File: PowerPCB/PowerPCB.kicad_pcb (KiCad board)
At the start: 2 copper layers, 41 parts, among them J1 Conn_01x03_Male, J2 Conn_01x10_Male, J5 Conn_01x07_Male, K1 1721081-5, K2 1721081-5, K3 1721081-5, Q1 Q_PMOS_DGS, U1 NCP1117-3.3_SOT223, U2 STM32F413ZHTx, U3 NCP1117-5.0_SOT223, U4 MCP2562-E-P, U5 MCP2562-E-P

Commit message: Testing branch
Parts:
- moved J5 30.6 mm to (171.4, 50.8)
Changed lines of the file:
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@@
     (solder_mask_min_width 0.25)
     (aux_axis_origin 0 0)
-    (visible_elements 7FFFFFFF)
+    (visible_elements 7FFFF7FF)
     (pcbplotparams
       (layerselection 0x010fc_ffffffff)
@@
   )
   (module Connector_PinHeader_2.54mm:PinHeader_1x07_P2.54mm_Horizontal (layer F.Cu)
-    (at 140.97 48.26)
+    (at 171.45 50.8)
     (descr "Through hole angled pin header, 1x07, 2.54mm pitch, 6mm pin length, single row")
     (tags "Through hole angled pin header THT 1x07 2.54mm single row")

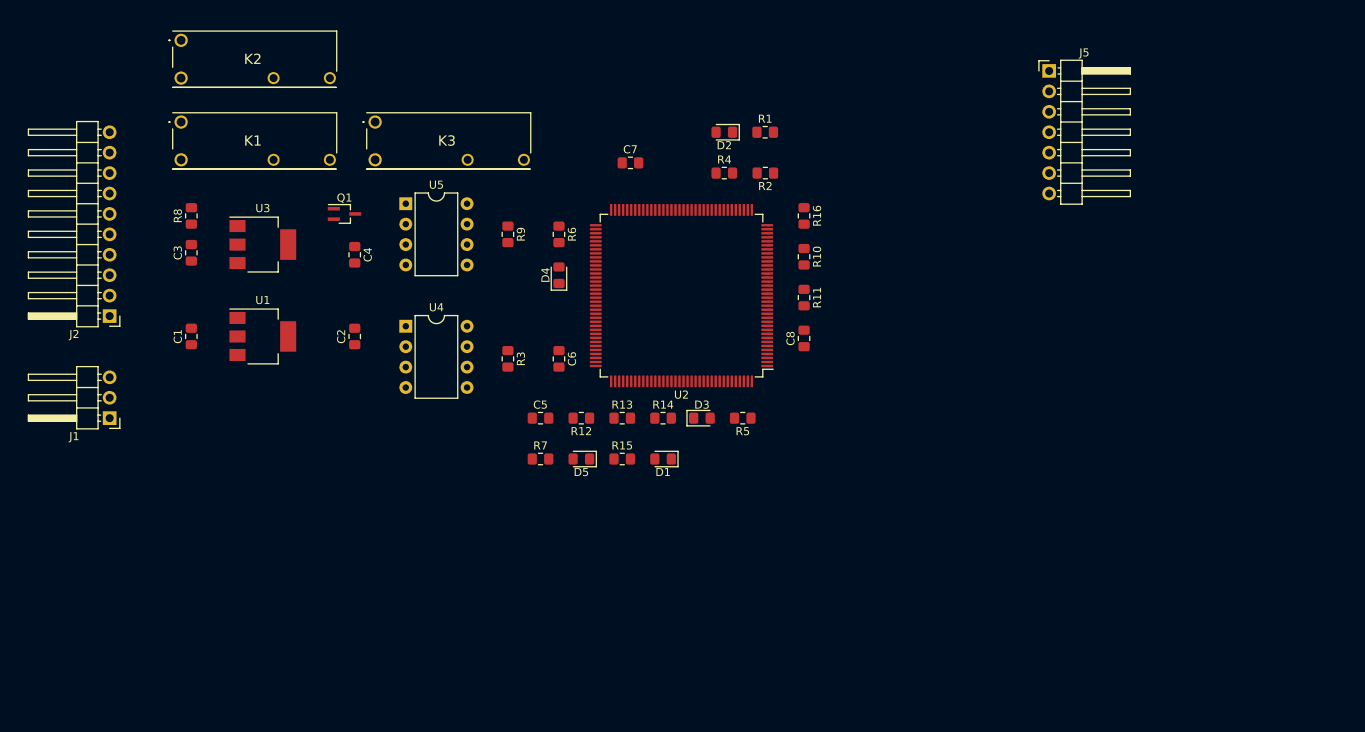
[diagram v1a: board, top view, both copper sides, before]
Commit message: Imported input protection components to PCBnew
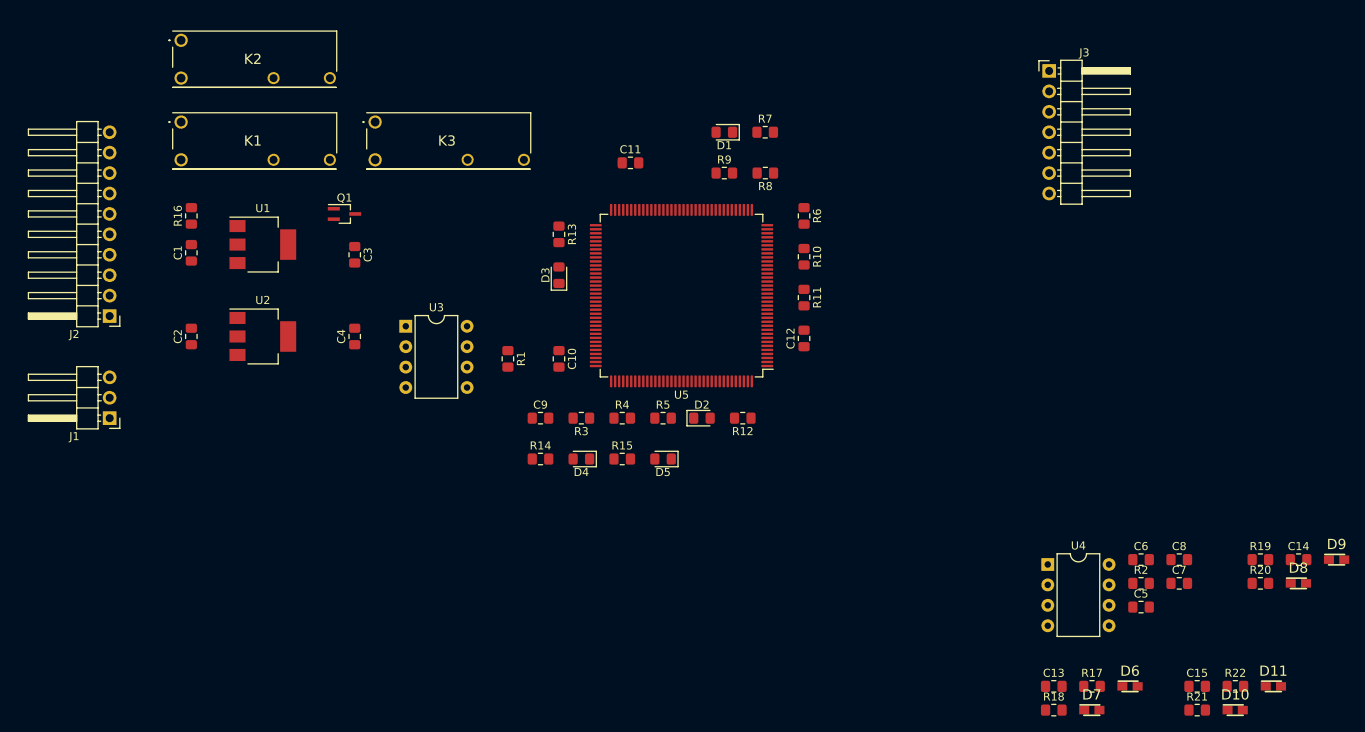
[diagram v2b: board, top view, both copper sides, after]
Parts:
- removed the R9 at (104.1, 71.1)
- removed the U5 at (91.4, 67.3)
- added C13: 10u, Capacitor_SMD:C_0805_2012Metric_Pad1.15x1.40mm_HandSolder, F.Cu at (172.0, 127.3)
- added C14: 10u, Capacitor_SMD:C_0805_2012Metric_Pad1.15x1.40mm_HandSolder, F.Cu at (202.5, 111.6)
- added C15: 10u, Capacitor_SMD:C_0805_2012Metric_Pad1.15x1.40mm_HandSolder, F.Cu at (189.9, 127.3)
- added C5: 0.1u, Capacitor_SMD:C_0805_2012Metric_Pad1.15x1.40mm_HandSolder, F.Cu at (182.9, 117.5)
- added C6: 0.1u, Capacitor_SMD:C_0805_2012Metric_Pad1.15x1.40mm_HandSolder, F.Cu at (182.9, 111.6)
- added C7: 0.1u, Capacitor_SMD:C_0805_2012Metric_Pad1.15x1.40mm_HandSolder, F.Cu at (187.6, 114.5)
- added C8: 0.1u, Capacitor_SMD:C_0805_2012Metric_Pad1.15x1.40mm_HandSolder, F.Cu at (187.6, 111.6)
- added D10: SD0805S040S0R1, SamacSys_Parts:DIOM2013X100N, F.Cu at (194.6, 130.3)
- added D11: SD0805S040S0R1, SamacSys_Parts:DIOM2013X100N, F.Cu at (199.3, 127.3)
- added D6: SD0805S040S0R1, SamacSys_Parts:DIOM2013X100N, F.Cu at (181.5, 127.3)
- added D7: SD0805S040S0R1, SamacSys_Parts:DIOM2013X100N, F.Cu at (176.8, 130.3)
- added D8: SD0805S040S0R1, SamacSys_Parts:DIOM2013X100N, F.Cu at (202.4, 114.5)
- added D9: SD0805S040S0R1, SamacSys_Parts:DIOM2013X100N, F.Cu at (207.2, 111.6)
- added R17: 10, Resistor_SMD:R_0805_2012Metric_Pad1.15x1.40mm_HandSolder, F.Cu at (176.8, 127.3)
- added R18: 1k, Resistor_SMD:R_0805_2012Metric_Pad1.15x1.40mm_HandSolder, F.Cu at (172.0, 130.3)
- added R19: 10, Resistor_SMD:R_0805_2012Metric_Pad1.15x1.40mm_HandSolder, F.Cu at (197.7, 111.6)
- added R2: 120, Resistor_SMD:R_0805_2012Metric_Pad1.15x1.40mm_HandSolder, F.Cu at (182.9, 114.5)
- added R20: 1k, Resistor_SMD:R_0805_2012Metric_Pad1.15x1.40mm_HandSolder, F.Cu at (197.7, 114.5)
- added R21: 10, Resistor_SMD:R_0805_2012Metric_Pad1.15x1.40mm_HandSolder, F.Cu at (189.9, 130.3)
- added R22: 1k, Resistor_SMD:R_0805_2012Metric_Pad1.15x1.40mm_HandSolder, F.Cu at (194.6, 127.3)
- added U4: MCP2562-E-P, Package_DIP:DIP-8_W7.62mm, F.Cu at (171.3, 112.2)
- C1: renamed from C3; value C -> 0.1u
- C2: renamed from C1; value C -> 0.1u
- C3: renamed from C4; value C -> 0.1u
- C4: renamed from C2; value C -> 0.1u
- renumbered C6 to C10, C7 to C11, C8 to C12, C5 to C9, D2 to D1, D3 to D2, D4 to D3, D5 to D4, D1 to D5, J5 to J3, R3 to R1, R5 to R12, R6 to R13, R7 to R14, R8 to R16, R12 to R3, R13 to R4, R14 to R5, R16 to R6, R1 to R7, R2 to R8, R4 to R9, U3 to U1, U1 to U2, U4 to U3, U2 to U5
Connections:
- R10 pad 2: Net-(R10-Pad2) -> /InputProtection3/Vin
- R11 pad 1: Net-(R10-Pad2) -> /InputProtection3/Vin
- R4 pad 2: Net-(R13-Pad2) -> /InputProtection/Vin
- R5 pad 1: Net-(R13-Pad2) -> /InputProtection/Vin
- R7 pad 2: Net-(R1-Pad2) -> /InputProtection2/Vin
- R8 pad 1: Net-(R1-Pad2) -> /InputProtection2/Vin
- U5 pad 124: Net-(R13-Pad2) -> /InputProtection/ToSTM
- U5 pad 26: Net-(R10-Pad2) -> /InputProtection3/ToSTM
- U5 pad 37: Net-(R1-Pad2) -> /InputProtection2/ToSTM

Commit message: Placed all input protection circuitry components in PCBnew
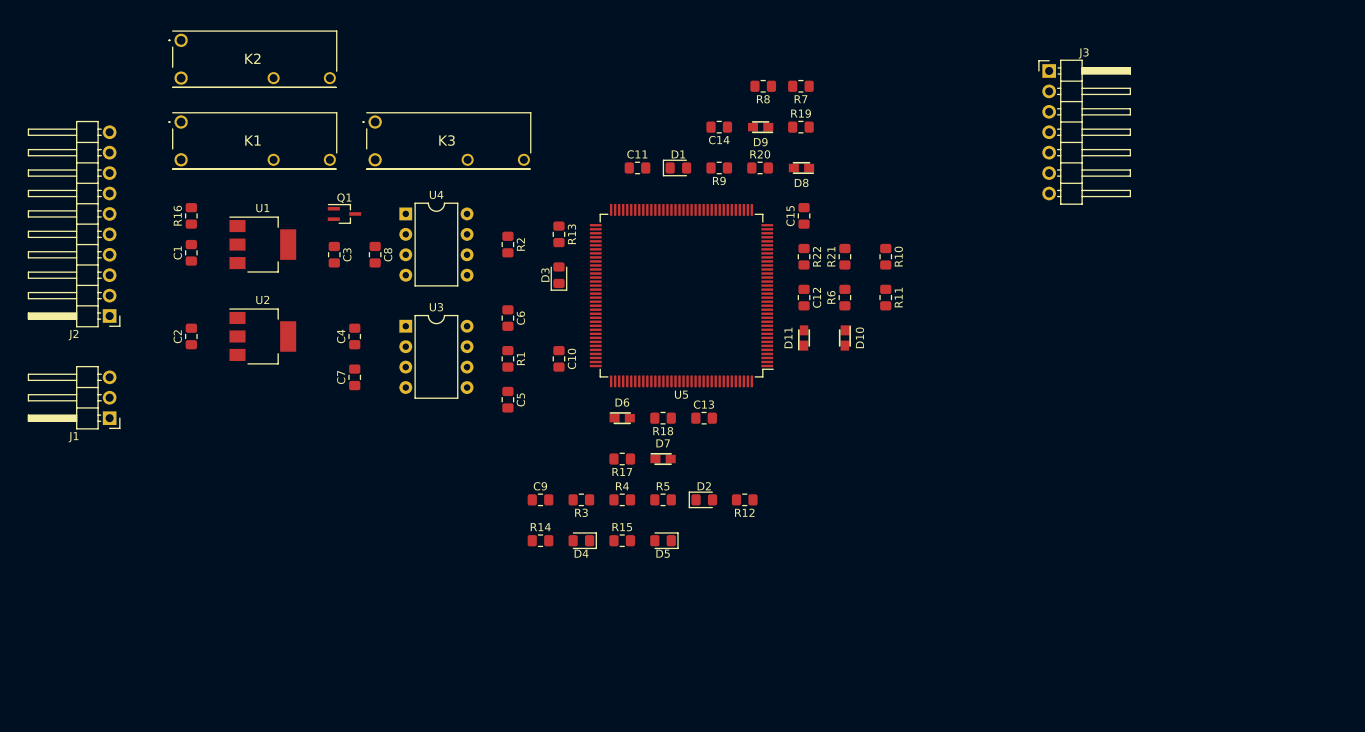
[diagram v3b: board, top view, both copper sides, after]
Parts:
- moved C8 106.9 mm to (87.6, 73.7), turned to 270 degrees
- moved C7 105.7 mm to (85.1, 88.9), turned to 90 degrees
- moved U4 91.0 mm to (91.4, 68.6)
- moved C14 89.9 mm to (130.4, 57.8), turned to 180 degrees
- moved D9 89.6 mm to (135.6, 57.8), turned to 180 degrees
- moved R2 89.3 mm to (104.1, 72.4), turned to 270 degrees
- moved C6 84.3 mm to (104.1, 81.5), turned to 270 degrees
- moved C5 82.9 mm to (104.1, 91.7), turned to 270 degrees
- moved R20 80.9 mm to (135.5, 62.9)
- moved D8 80.5 mm to (140.7, 62.9), turned to 180 degrees
- moved R19 78.5 mm to (140.6, 57.8)
- moved C15 76.2 mm to (141.0, 68.8), turned to 90 degrees
- moved R22 75.7 mm to (141.0, 73.9), turned to 270 degrees
- moved D11 72.7 mm to (141.0, 84.0), turned to 90 degrees
- moved D6 71.4 mm to (118.4, 94.0)
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
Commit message: Added edge cuts
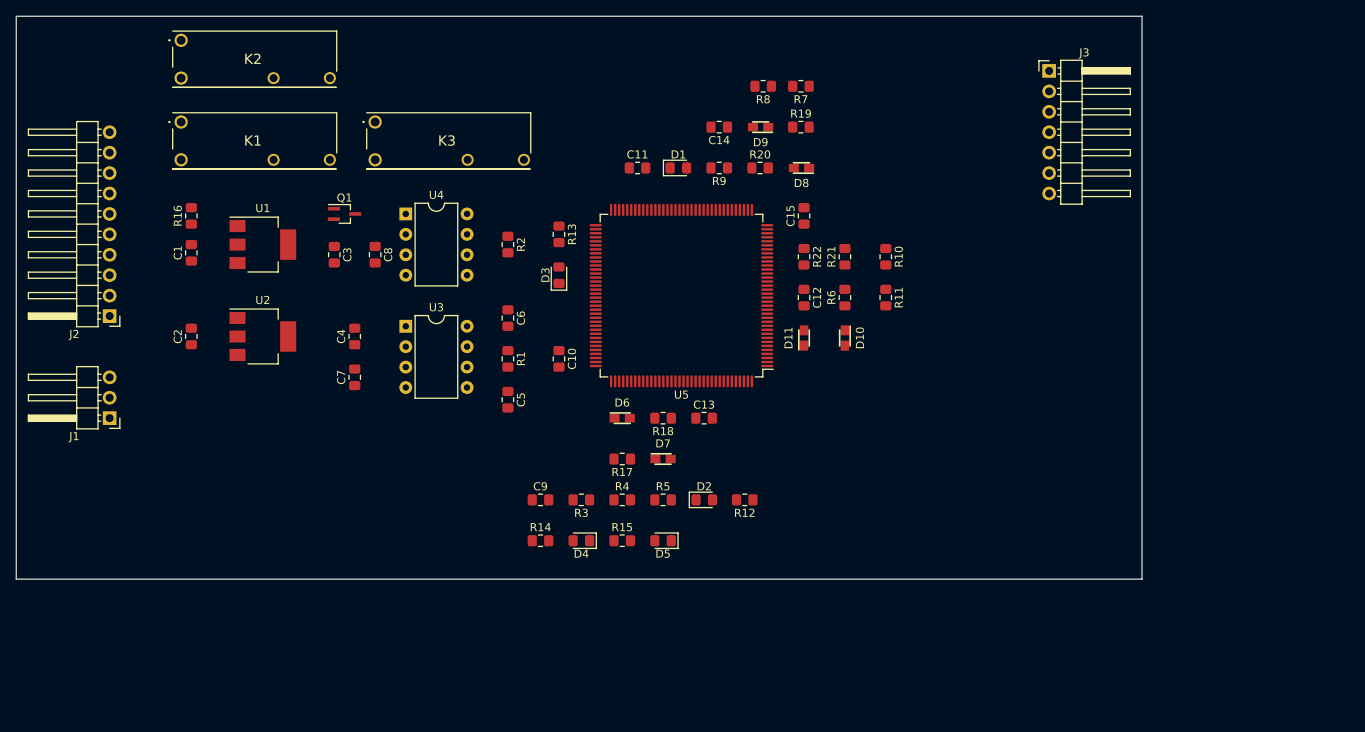
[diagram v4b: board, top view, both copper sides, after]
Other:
- board outline added: 140 x 70 mm
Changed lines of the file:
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@@
   (general
     (thickness 1.6)
-    (drawings 0)
+    (drawings 4)
     (tracks 0)
     (zones 0)
@@
   )
   (setup
-    (last_trace_width 0.25)
+    (last_trace_width 0.254)
+    (user_trace_width 0.254)
+    (user_trace_width 0.762)
     (trace_clearance 0.2)
     (zone_clearance 0.508)
@@
     )
   )
+  (gr_line (start 183 44) (end 43 44) (layer Edge.Cuts) (width 0.05))
+  (gr_line (start 183 114) (end 183 44) (layer Edge.Cuts) (width 0.05))
+  (gr_line (start 43 114) (end 183 114) (layer Edge.Cuts) (width 0.05))
+  (gr_line (start 43 44) (end 43 114) (layer Edge.Cuts) (width 0.05))
 )

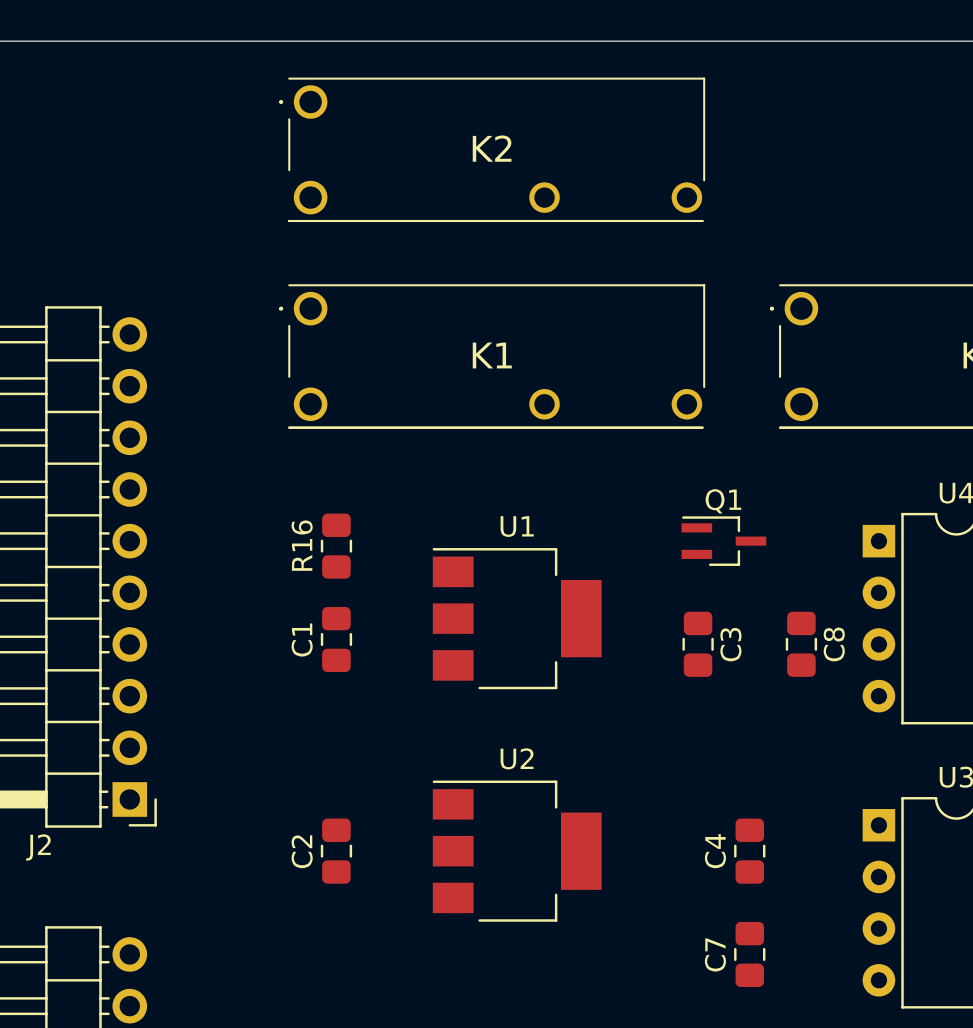
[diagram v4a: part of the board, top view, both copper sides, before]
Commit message: Routed all of VCC_12
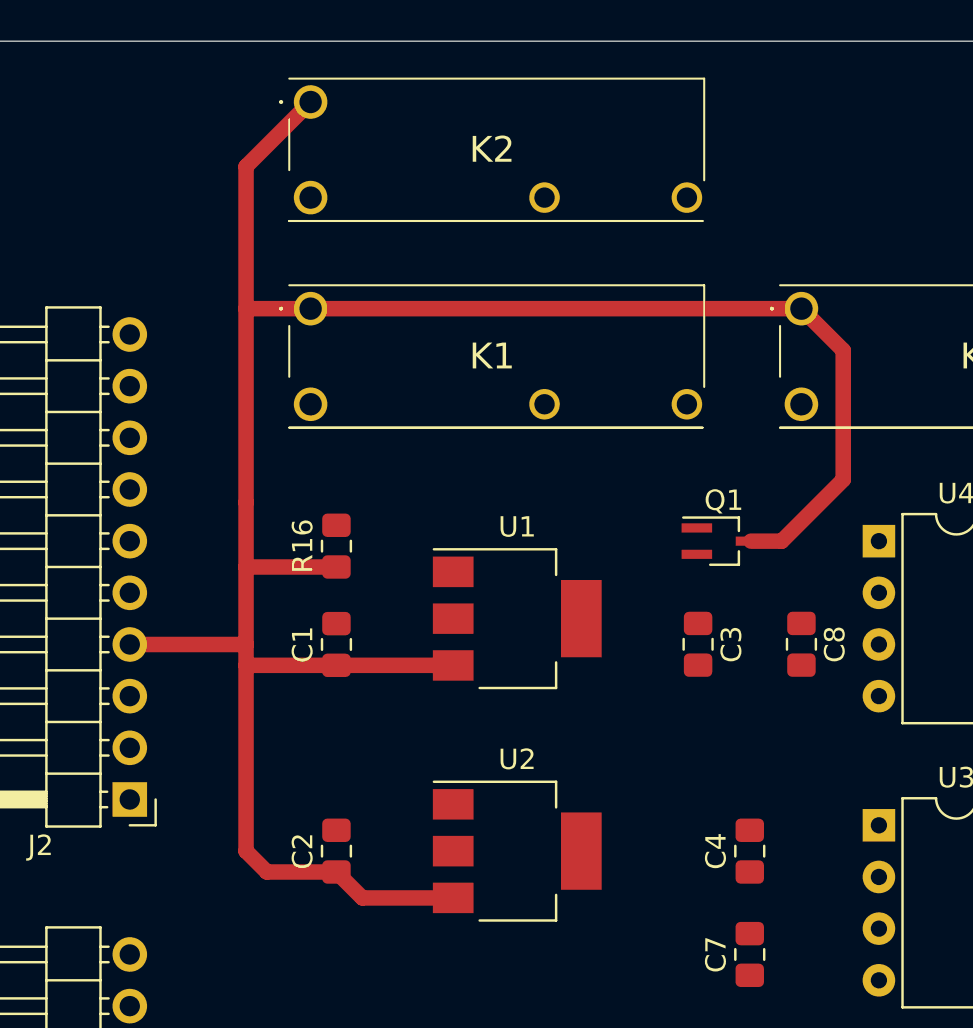
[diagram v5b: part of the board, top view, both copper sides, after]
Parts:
- moved C1 0.24 mm to (64.8, 73.7)
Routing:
- net VCC_12: track 0.00 -> 112.0 mm
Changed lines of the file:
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@@
     (thickness 1.6)
     (drawings 4)
-    (tracks 0)
+    (tracks 21)
     (zones 0)
     (modules 60)
@@
   )
   (setup
-    (last_trace_width 0.254)
+    (last_trace_width 0.762)
     (user_trace_width 0.254)
     (user_trace_width 0.762)
@@
   )
   (module Capacitor_SMD:C_0805_2012Metric_Pad1.15x1.40mm_HandSolder locked (layer F.Cu)
-    (at 64.77 73.415 90)
+    (at 64.77 73.66 90)
     (descr "Capacitor SMD 0805 (2012 Metric), square (rectangular) end terminal, IPC_7351 nominal with elongated pad for handsoldering. (Body size source: https://docs.google.com/spreadsheets/d/1BsfQQcO9C6DZCsRaXUlFlo91Tg2WpOkGARC1WS5S8t0/edit?usp=sharing), generated with kicad-footprint-generator")
     (tags "capacitor handsolder")
@@
   (gr_line (start 43 114) (end 183 114) (layer Edge.Cuts) (width 0.05))
   (gr_line (start 43 44) (end 43 114) (layer Edge.Cuts) (width 0.05))
+  (segment (start 70.505 74.685) (end 70.51 74.69) (width 0.762) (layer F.Cu) (net 2))
+  (segment (start 64.77 74.685) (end 70.505 74.685) (width 0.762) (layer F.Cu) (net 2))
+  (segment (start 66.045 86.12) (end 70.51 86.12) (width 0.762) (layer F.Cu) (net 2))
+  (segment (start 64.77 84.845) (end 66.045 86.12) (width 0.762) (layer F.Cu) (net 2))
+  (segment (start 60.325 50.165) (end 63.5 46.99) (width 0.762) (layer F.Cu) (net 2))
+  (segment (start 63.5 57.15) (end 60.325 57.15) (width 0.762) (layer F.Cu) (net 2))
+  (segment (start 60.325 66.675) (end 60.325 57.15) (width 0.762) (layer F.Cu) (net 2))
+  (segment (start 60.325 57.15) (end 60.325 50.165) (width 0.762) (layer F.Cu) (net 2))
+  (segment (start 60.325 69.85) (end 64.77 69.85) (width 0.762) (layer F.Cu) (net 2))
+  (segment (start 60.325 69.85) (end 60.325 66.675) (width 0.762) (layer F.Cu) (net 2))
+  (segment (start 61.35 84.845) (end 64.77 84.845) (width 0.762) (layer F.Cu) (net 2))
+  (segment (start 60.325 83.82) (end 61.35 84.845) (width 0.762) (layer F.Cu) (net 2))
+  (segment (start 54.61 73.66) (end 60.325 73.66) (width 0.762) (layer F.Cu) (net 2))
+  (segment (start 60.325 69.85) (end 60.325 73.66) (width 0.762) (layer F.Cu) (net 2))
+  (segment (start 60.325 73.66) (end 60.325 83.82) (width 0.762) (layer F.Cu) (net 2))
+  (segment (start 64.77 74.685) (end 60.325 74.685) (width 0.762) (layer F.Cu) (net 2))
+  (segment (start 63.5 57.15) (end 87.63 57.15) (width 0.762) (layer F.Cu) (net 2))
+  (segment (start 85.15 68.58) (end 86.662 68.58) (width 0.762) (layer F.Cu) (net 2))
+  (segment (start 86.662 68.58) (end 89.686 65.556) (width 0.762) (layer F.Cu) (net 2))
+  (segment (start 89.686 59.206) (end 87.63 57.15) (width 0.762) (layer F.Cu) (net 2))
+  (segment (start 89.686 65.556) (end 89.686 59.206) (width 0.762) (layer F.Cu) (net 2))
 )
